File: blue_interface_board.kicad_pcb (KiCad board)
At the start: 4 copper layers, 70 x 70 mm, 117 parts, among them J1 Conn_01x05, J2 USB_B_Micro, J3 ESTOP, J4 PWR, J5 Conn_ARM_JTAG_SWD_10, J6 DNP, J7 FAN, Q1 MMBT5401LT1G, Q2 Q_NMOS_GDS, Q3 MMBT3904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

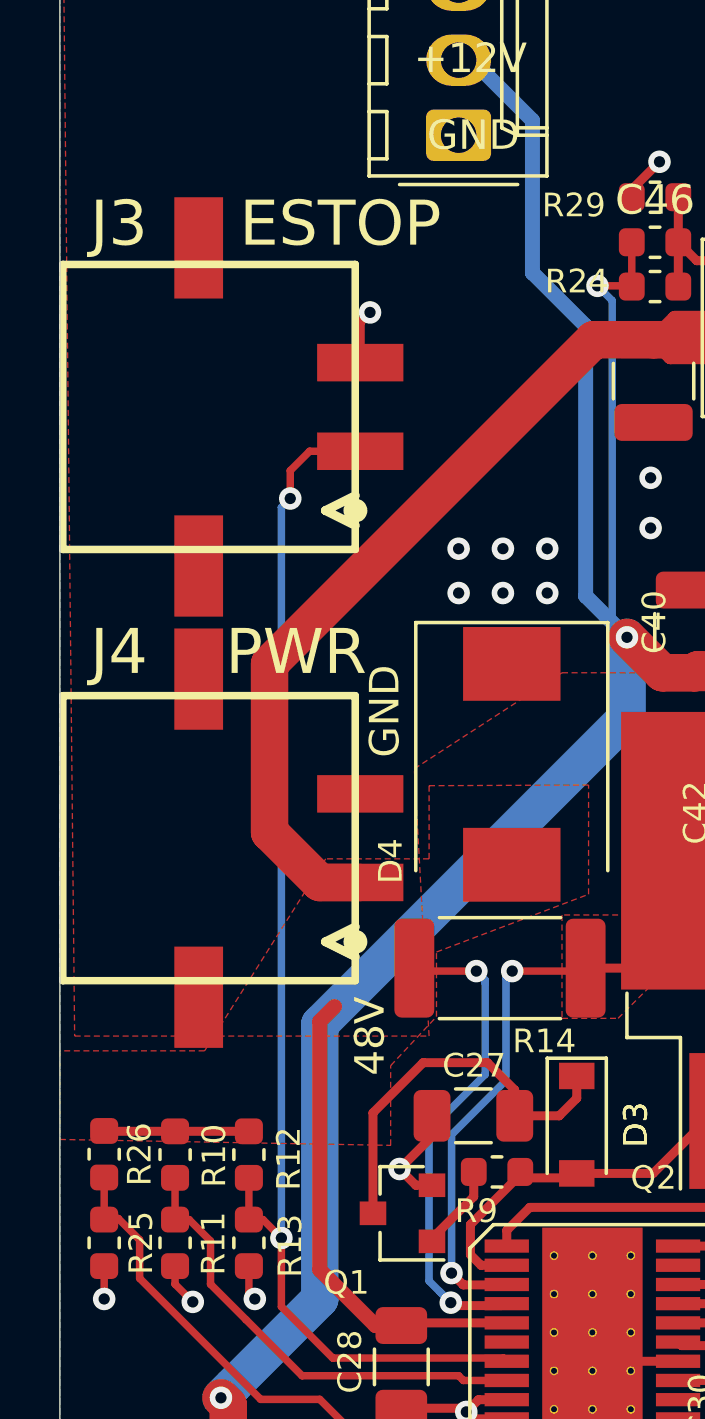
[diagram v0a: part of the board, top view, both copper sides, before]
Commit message: Reverted to nanofit for e-stop
Signed-off-by: Luca Della Vedova <luca@openrobotics.org>
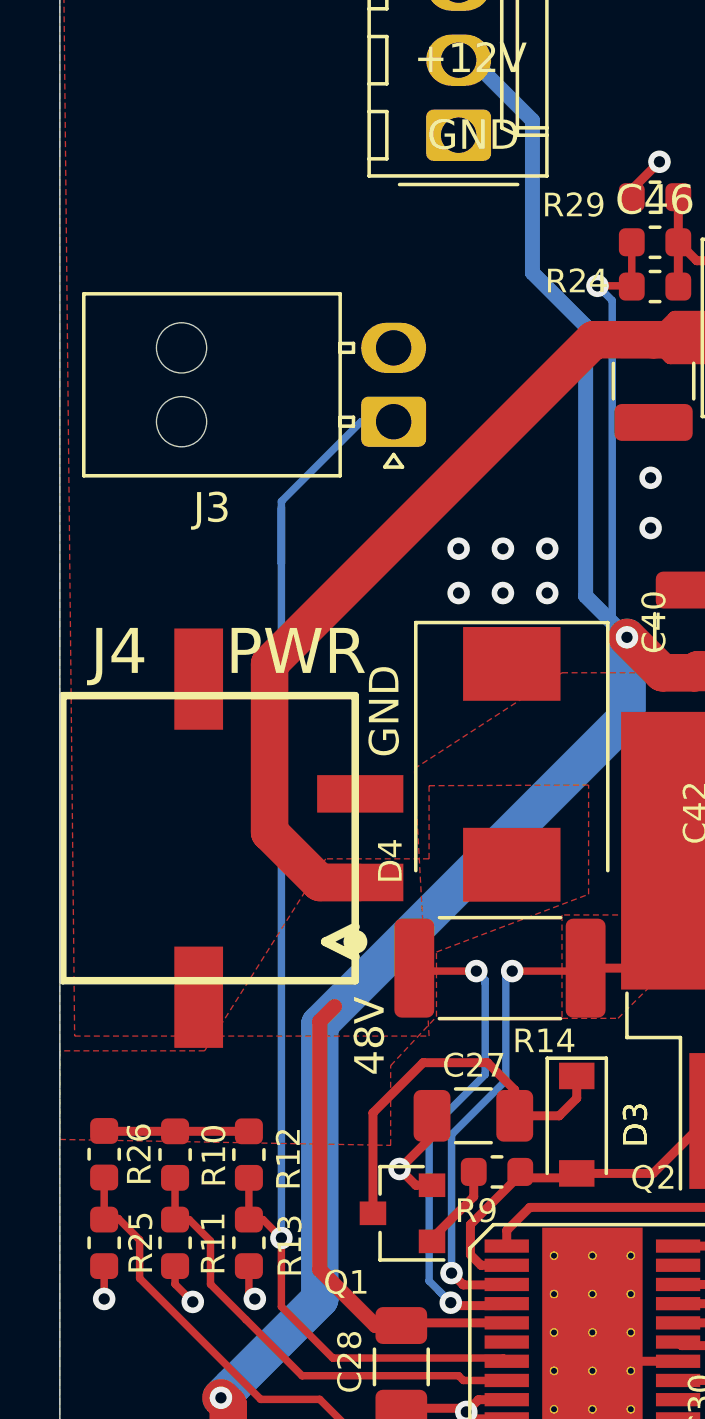
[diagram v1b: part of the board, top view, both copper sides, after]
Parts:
- J3: footprint BLDC:molex-0436500213 -> Connector_Molex:Molex_Nano-Fit_105313-xx02_1x02_P2.50mm_Horizontal
- moved J3 11.2 mm to (100.3, 86.7), turned to 180 degrees
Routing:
- net Net-(J3-Pad1): track 42.2 -> 45.2 mm, vias 2 -> 1
- net GNDPWR: track 78.0 -> 76.2 mm, vias 53 -> 52

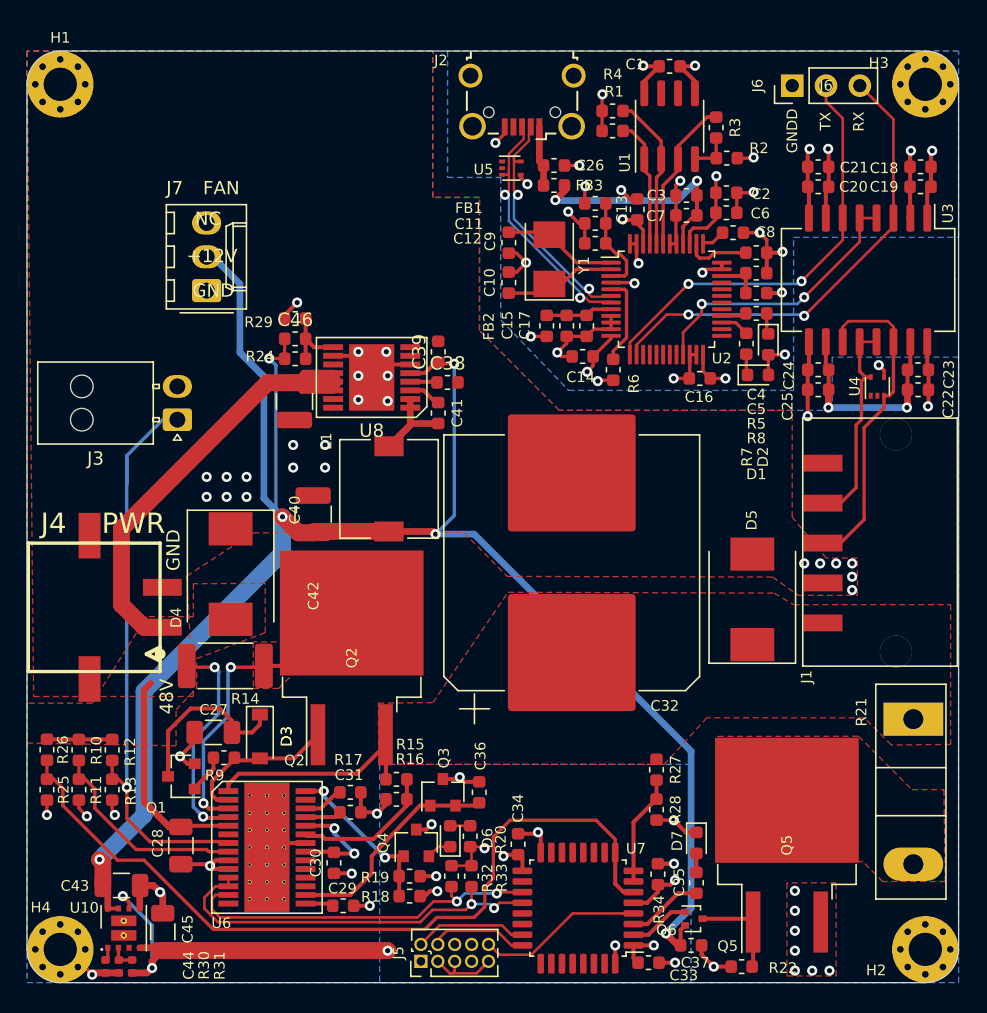
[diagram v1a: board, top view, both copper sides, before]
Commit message: Changed USB connector to be on same side
Signed-off-by: Luca Della Vedova <luca@openrobotics.org>
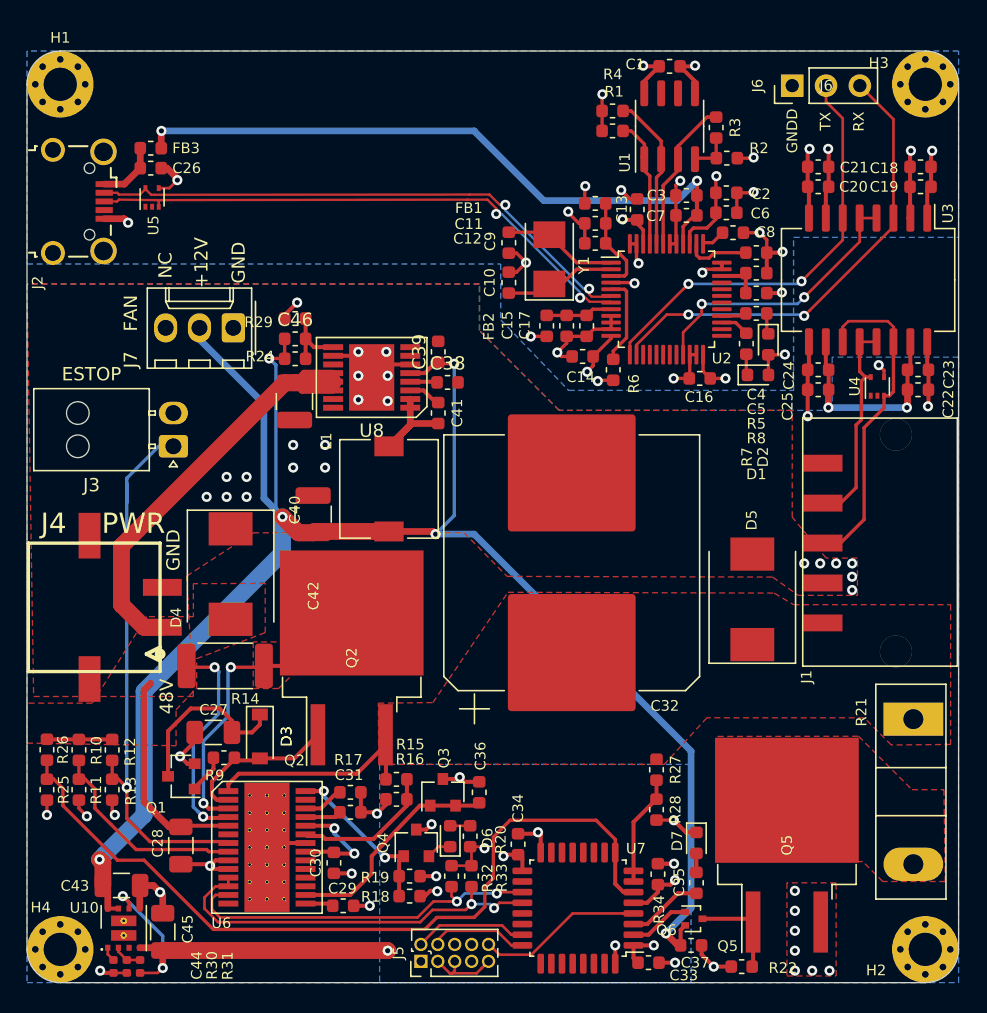
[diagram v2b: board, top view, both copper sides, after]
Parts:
- R17: value 47k -> 240k
- moved J2 34.1 mm to (92.9, 70.3), turned to -90 degrees
- moved FB3 30.4 mm to (98.3, 66.3)
- moved C26 30.3 mm to (98.3, 67.8)
- moved U5 27.1 mm to (98.4, 70.0), turned to 90 degrees
- moved J7 3.44 mm to (104.5, 79.8), turned to 180 degrees
- moved J3 2.02 mm to (100.0, 88.7)
- moved C44 0.60 mm to (95.5, 127.8)
- moved R30 0.60 mm to (97.5, 127.8)
- moved R31 0.60 mm to (96.5, 127.8)
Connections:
- H1 pad 1: GNDPWR -> Net-(H1-Pad1)
- H2 pad 1: GNDPWR -> Net-(H2-Pad1)
- H4 pad 1: GNDPWR -> Net-(H4-Pad1)
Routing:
- net +5V: track 17.8 -> 49.5 mm
- net /Comms/DN: track 18.5 -> 42.3 mm
- net /Comms/DP: track 19.0 -> 42.3 mm
- net +12V: track 146.0 -> 140.6 mm
- net Net-(J3-Pad1): track 45.2 -> 42.6 mm
- net GNDPWR: track 76.2 -> 74.1 mm, vias 52 -> 51
- net GNDD: track 56.9 -> 58.6 mm, vias 19 -> 18
- net /Power/VIN: track 74.3 -> 73.6 mm
- added copper zone on B.Cu, net +12V
- removed copper zone on B.Cu, net GNDPWR

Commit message: add rs485 termination, change to SOT-323 TVS diodes, various OCD
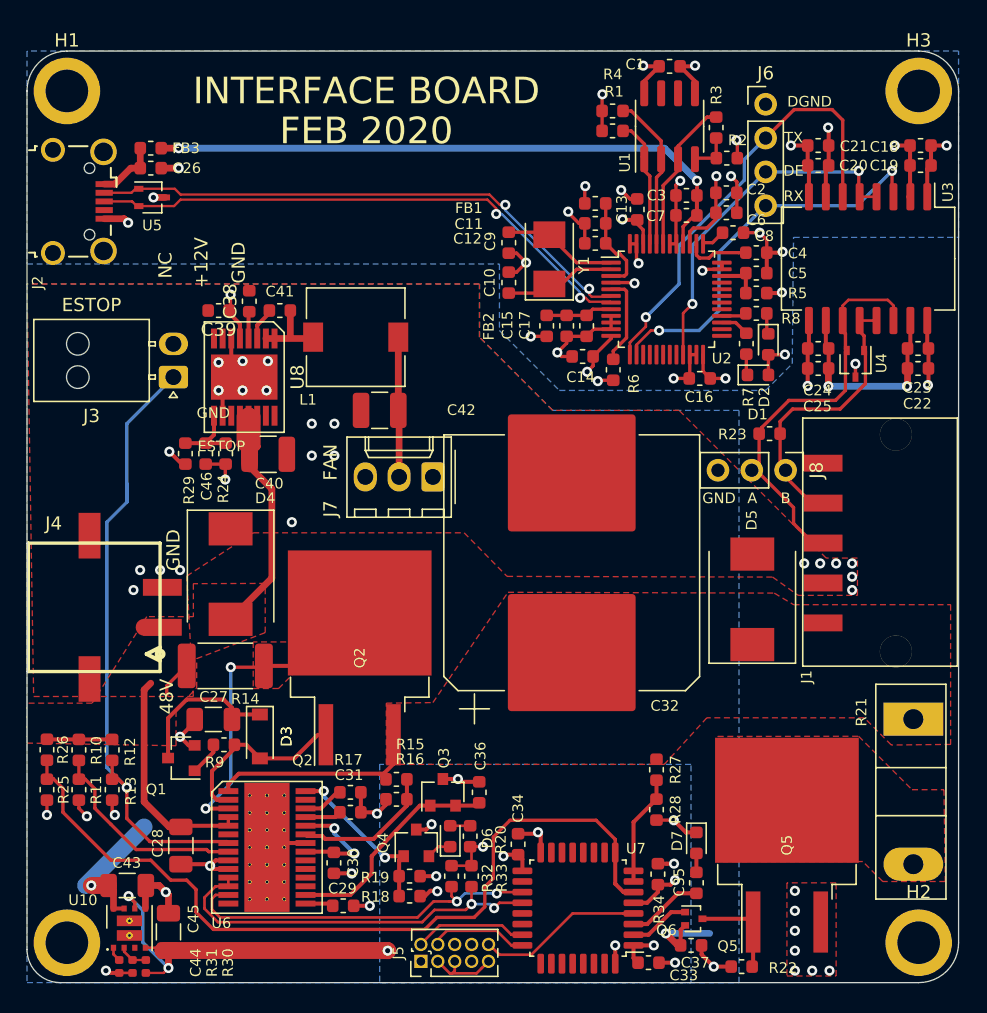
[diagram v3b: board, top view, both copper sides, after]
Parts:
- added J8: power-side RS485 debug/expansion, Connector_PinHeader_2.54mm:PinHeader_1x03_P2.54mm_Vertical, F.Cu at (146.0, 90.5)
- added R23: 120, Resistor_SMD:R_0603_1608Metric, F.Cu at (144.8, 87.8)
- H1, H2, H3, H4: footprint MountingHole:MountingHole_2.5mm_Pad_Via -> MountingHole:MountingHole_3.2mm_M3_DIN965_Pad
- J1: value Conn_01x05 -> arm connector
- J6: value DNP -> logic-side RS485 debug/expansion; footprint Connector_PinHeader_2.54mm:PinHeader_1x03_P2.54mm_Vertical -> Connector_PinHeader_2.54mm:PinHeader_1x04_P2.54mm_Vertical
- U4, U5: value TPD2E2U06 -> TPD2E2U06DCK; footprint Package_TO_SOT_SMD:SOT-553 -> Package_TO_SOT_SMD:SOT-323_SC-70
- moved J7 18.7 mm to (119.5, 91.0)
- moved C39 16.8 mm to (103.4, 78.5), turned to 180 degrees
- moved C38 16.1 mm to (105.7, 77.8), turned to 90 degrees
- moved C41 14.2 mm to (108.0, 78.5), turned to 0 degrees
- moved R29 13.1 mm to (100.9, 89.2), turned to -90 degrees
- moved L1 11.7 mm to (113.7, 80.5), turned to 0 degrees
- moved C46 10.9 mm to (102.4, 89.2), turned to 90 degrees
- moved U8 9.58 mm to (105.3, 83.5), turned to 180 degrees
- moved C42 9.26 mm to (115.5, 86.0), turned to 180 degrees
- moved R24 8.84 mm to (103.9, 89.2), turned to 90 degrees
- moved J3 5.20 mm to (100.0, 83.5)
- moved C40 4.44 mm to (107.1, 89.3), turned to 0 degrees
- moved J6 2.44 mm to (144.5, 63.0), turned to 0 degrees
- moved U4 2.37 mm to (151.2, 82.5), turned to -90 degrees
- moved C18 1.60 mm to (156.1, 66.1)
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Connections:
- C22 pad 2: GNDPWR -> GND
- C23 pad 2: GNDPWR -> GND
- C24 pad 2: GNDPWR -> GND
- C25 pad 2: GNDPWR -> GND
- C27 pad 2: GNDPWR -> GND
- C28 pad 2: GNDPWR -> GND
- C29 pad 2: GNDPWR -> GND
- C30 pad 2: GNDPWR -> GND
- C31 pad 2: GNDPWR -> GND
- C32 pad 2: GNDPWR -> GND
- C33 pad 2: GNDPWR -> GND
- C34 pad 2: GNDPWR -> GND
- C35 pad 2: GNDPWR -> GND
- C36 pad 2: GNDPWR -> GND
- C37 pad 2: GNDPWR -> GND
- C38 pad 2: GNDPWR -> GND
- C39 pad 2: GNDPWR -> GND
- C40 pad 2: GNDPWR -> GND
- C42 pad 2: GNDPWR -> GND
- C43 pad 1: GNDPWR -> GND
- C44 pad 1: GNDPWR -> GND
- C45 pad 2: GNDPWR -> GND
- D4 pad 1: GNDPWR -> GND
- D5 pad 2: GNDPWR -> GND
- D7 pad 1: GNDPWR -> GND
- J1 pad 4: GNDPWR -> GND
- J3 pad 2: GNDPWR -> GND
- J4 pad 2: GNDPWR -> GND
- J4 pad 3: GNDPWR -> GND
- J4 pad 4: GNDPWR -> GND
- J5 pad 3: GNDPWR -> GND
- J5 pad 5: GNDPWR -> GND
- J5 pad 9: GNDPWR -> GND
- J6 pad 3: /Comms/RS485_RX -> /Comms/RS485_DE
- J7 pad 1: GNDPWR -> GND
- Q1 pad 2: GNDPWR -> GND
- Q3 pad 3: GNDPWR -> GND
- Q4 pad 3: GNDPWR -> GND
- Q5 pad 3: GNDPWR -> GND
- R11 pad 2: GNDPWR -> GND
- R13 pad 2: GNDPWR -> GND
- R16 pad 2: GNDPWR -> GND
- R17 pad 2: GNDPWR -> GND
- R19 pad 2: GNDPWR -> GND
- R22 pad 2: GNDPWR -> GND
- R25 pad 2: GNDPWR -> GND
- R28 pad 2: GNDPWR -> GND
- R29 pad 2: GNDPWR -> GND
- R31 pad 2: GNDPWR -> GND
- U10 pad 5: GNDPWR -> GND
- U10 pad 9: GNDPWR -> GND
- U3 pad 16: GNDPWR -> GND
- U3 pad 9: GNDPWR -> GND
- U4 pad 1: Net-(U4-Pad1) -> /Comms/RS485_B
- U4 pad 2: Net-(U4-Pad2) -> /Comms/RS485_A
- U4 pad 3: /Comms/RS485_A -> GND
- U5 pad 1: Net-(U5-Pad1) -> /Comms/DN
- U5 pad 2: Net-(U5-Pad2) -> /Comms/DP
- U5 pad 3: /Comms/DP -> GNDD
- U6 pad 10: GNDPWR -> GND
- U6 pad 22: GNDPWR -> GND
- U6 pad 29: GNDPWR -> GND
- U6 pad 9: GNDPWR -> GND
- U7 pad 16: GNDPWR -> GND
- U7 pad 32: GNDPWR -> GND
- U8 pad 10: GNDPWR -> GND
- U8 pad 15: GNDPWR -> GND
- U8 pad 16: GNDPWR -> GND
- U8 pad 17: GNDPWR -> GND
- U8 pad 6: GNDPWR -> GND
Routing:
- net +12V: track 140.6 -> 33.4 mm, vias 6 -> 4
- net GNDPWR: track 74.1 -> 0.00 mm, vias 51 -> 0
- net GND: track 0.00 -> 72.3 mm, vias 0 -> 51
- net /Power/VIN: track 73.6 -> 50.4 mm, vias 2 -> 0
- net /Comms/RS485_A: track 25.3 -> 34.6 mm
- net /Comms/RS485_B: track 16.5 -> 24.3 mm
- net Net-(J3-Pad1): track 42.6 -> 48.4 mm
- net /Comms/RS485_RX: track 35.4 -> 29.9 mm
- net /Comms/RS485_DE: track 21.2 -> 26.6 mm
- net +5V: track 49.5 -> 46.4 mm
- net Net-(C41-Pad2): track 8.62 -> 5.58 mm
- net VOUT: track 20.3 -> 18.2 mm
- net /Power/GATE: track 11.8 -> 13.5 mm
- net Net-(C27-Pad1): track 13.3 -> 11.8 mm
- net Net-(R25-Pad1): track 61.3 -> 62.6 mm
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- added copper zone on In2.Cu, net +3V3
- added copper zone on F.Cu, net GND
- added copper zone on In1.Cu, net GND
- added copper zone on In2.Cu, net GND
- added copper zone on In1.Cu, net GNDD
- removed copper zone on In1.Cu, net +3V3
- removed copper zone on In2.Cu, net GNDD
- removed copper zone on F.Cu, net GNDPWR
- removed copper zone on In1.Cu, net GNDPWR
- removed copper zone on In2.Cu, net GNDPWR
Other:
- outline, holes or cut-outs redrawn
- board text added: "A"
- board text added: "B"
- board text added: "DE"
- board text added: "DGND"
- board text added: "ESTOP"
- board text added: "FEB 2020"
- board text added: "INTERFACE BOARD"
- board text removed: "GNDD"

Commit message: working through the power subsystems now. changed e-stop topology.
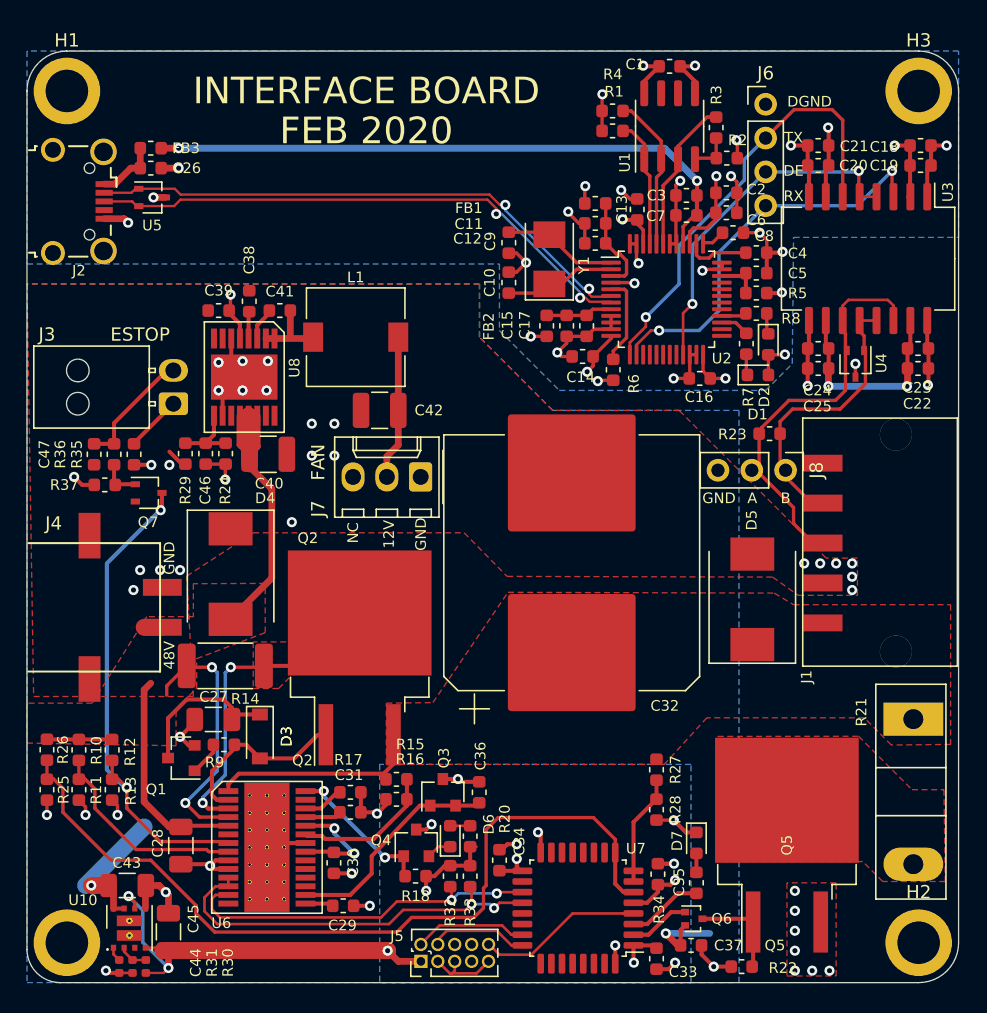
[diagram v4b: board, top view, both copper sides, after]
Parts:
- removed R19: 1M, Resistor_SMD:R_0603_1608Metric
- added C47: 100n, Capacitor_SMD:C_0603_1608Metric, F.Cu at (94.0, 89.3)
- added Q7: NTS4001NT1G, Package_TO_SOT_SMD:SOT-323_SC-70, F.Cu at (98.1, 92.2)
- added R35: 1k, Resistor_SMD:R_0603_1608Metric, F.Cu at (97.0, 89.3)
- added R36: 10k, Resistor_SMD:R_0603_1608Metric, F.Cu at (95.5, 89.3)
- added R37: 100k, Resistor_SMD:R_0603_1608Metric, F.Cu at (94.8, 91.6)
- D4: value 5.0SMDJ51A -> 5.0SMDJ60A
- R11: value 6.65k -> 6k65
- R13: value 25.5k -> 25k5
- R14: value 15m -> 10m
- moved J3 2.00 mm to (100.0, 85.5)
- moved C34 1.84 mm to (124.5, 119.8)
- moved R18 1.57 mm to (118.2, 121.0)
- moved J7 0.92 mm to (118.6, 91.0)
- moved C33 0.67 mm to (136.3, 127.2), turned to -90 degrees
- moved R32 0.10 mm to (120.8, 121.0)
- moved R33 0.10 mm to (122.3, 121.0)
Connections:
- J3 pad 2: GND -> Net-(C47-Pad1)
- R12 pad 2: Net-(J3-Pad1) -> Net-(Q7-Pad3)
- R13 pad 1: Net-(J3-Pad1) -> Net-(Q7-Pad3)
- U6 pad 7: Net-(J3-Pad1) -> Net-(Q7-Pad3)
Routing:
- net Net-(J3-Pad1): track 48.4 -> 4.24 mm, vias 1 -> 0
- net Net-(Q7-Pad3): track 0.00 -> 37.6 mm, vias 0 -> 2
- net /Power/VIN: track 50.4 -> 66.7 mm, vias 0 -> 2
- net Net-(C47-Pad1): track 0.00 -> 9.15 mm
- net +3.3VP: track 45.1 -> 49.6 mm, vias 8 -> 7
- net Net-(Q7-Pad1): track 0.00 -> 3.08 mm
- net +12V: track 33.4 -> 35.2 mm, vias 4 -> 5
- net /Power/PGD: track 12.8 -> 11.3 mm
- net GND: track 72.3 -> 73.3 mm, vias 51 -> 52
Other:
- board text added: "12V"
- board text removed: "+12V"
- board text removed: "ESTOP"
